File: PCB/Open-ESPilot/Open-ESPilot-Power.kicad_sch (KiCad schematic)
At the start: 32 parts, among them J2 VOUT, J3 VIN, J4 GND, M1 Clone "MP1584" module, Q1 AO3401A, U2 AMS1117-3.3, U3 AMS1117-3.3, U4 INA219AxD

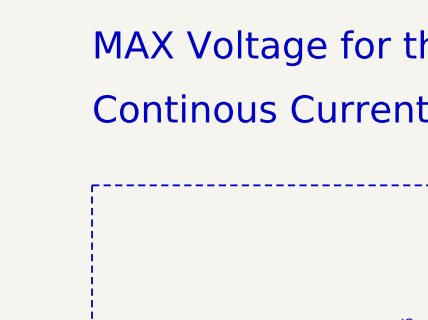
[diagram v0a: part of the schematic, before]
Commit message: Selected componets and tried to made a csv.
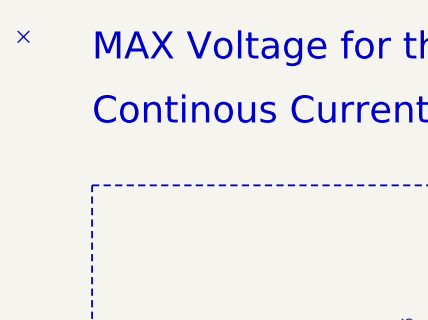
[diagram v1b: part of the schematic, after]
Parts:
- C12, C13, C14: LCSC (none) -> C49678
- C6, C7, C8, C9: LCSC (none) -> C5674
- J2, J3, J4, JP1, JP2, JP3: LCSC (none) -> -
- M1: LCSC (none) -> -; Non LCSC link (none) -> https://www.aliexpress.com/item/1005005870392716.html
- R10, R11, R12, R6: LCSC (none) -> C84376
- R5: LCSC (none) -> C84375
- R7, R9: LCSC (none) -> C96347
- U3: LCSC (none) -> C6186
- U4: LCSC (none) -> C1574856
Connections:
- no-connect marks 0 -> 1
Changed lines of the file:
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@@
 		(color 0 0 0 0)
 	)
+	(no_connect
+		(at 8.89 15.24)
+	)
 	(wire
 		(pts
@@
 			)
 		)
+		(property "LCSC" "C84376"
+			(at 261.62 58.42 0)
+			(effects
+				(font
+					(size 1.27 1.27)
+				)
+				(hide yes)
+			)
+		)
 		(pin "1"
 		)
@@
 			)
 		)
+		(property "LCSC" "-"
+			(at 270.51 73.66 90)
+			(effects
+				(font
+					(size 1.27 1.27)
+				)
+				(hide yes)
+			)
+		)
 		(pin "1"
 		)
@@
 			)
 		)
+		(property "LCSC" "-"
+			(at 54.61 81.28 0)
+			(effects
+				(font
+					(size 1.27 1.27)
+				)
+				(hide yes)
+			)
+		)
 		(pin "1"
 		)
@@
 			)
 		)
+		(property "LCSC" "C5674"
+			(at 69.85 129.54 0)
+			(effects
+				(font
+					(size 1.27 1.27)
+				)
+				(hide yes)
+			)
+		)
 		(pin "1"
 		)
@@
 			)
 		)
+		(property "LCSC" "C96347"
+			(at 209.55 41.91 0)
+			(effects
+				(font
+					(size 1.27 1.27)
+				)
+				(hide yes)
+			)
+		)
 		(pin "2"
 		)
@@
 			)
 		)
+		(property "LCSC" "C1574856"
+			(at 233.68 62.23 0)
+			(effects
+				(font
+					(size 1.27 1.27)
+				)
+				(hide yes)
+			)
+		)
 		(pin "6"
 		)
@@
 			)
 		)
+		(property "LCSC" "C49678"
+			(at 201.93 53.34 90)
+			(effects
+				(font
+					(size 1.27 1.27)
+				)
+				(hide yes)
+			)
+		)
 		(pin "1"
 		)
@@
 			)
 		)
+		(property "LCSC" "C5674"
+			(at 39.37 166.37 0)
+			(effects
+				(font
+					(size 1.27 1.27)
+				)
+				(hide yes)
+			)
+		)
 		(pin "1"
 		)
@@
 			)
 		)
+		(property "LCSC" "-"
+			(at 261.62 73.66 90)
+			(effects
+				(font
+					(size 1.27 1.27)
+				)
+				(hide yes)
+			)
+		)
 		(pin "1"
 		)
@@
 			)
 		)
-		(property "Datasheet" "https://www.aliexpress.com/item/1005005870392716.html"
+		(property "Datasheet" ""
 			(at 138.43 111.252 0)
 			(effects
@@
 			)
 		)
+		(property "LCSC" "-"
+			(at 138.43 123.19 0)
+			(effects
+				(font
+					(size 1.27 1.27)
+				)
+				(hide yes)
+			)
+		)
+		(property "Non LCSC link" "https://www.aliexpress.com/item/1005005870392716.html"
+			(at 138.43 123.19 0)
+			(effects
+				(font
+					(size 1.27 1.27)
+				)
+				(hide yes)
+			)
+		)
 		(pin "3"
 		)
@@
 			)
 		)
+		(property "LCSC" "-"
+			(at 201.93 137.16 0)
+			(effects
+				(font
+					(size 1.27 1.27)
+				)
+				(hide yes)
+			)
+		)
 		(pin "1"
 		)
@@
 			)
 		)
+		(property "LCSC" "C5674"
+			(at 69.85 166.37 0)
+			(effects
+				(font
+					(size 1.27 1.27)
+				)
+				(hide yes)
+			)
+		)
 		(pin "1"
 		)
@@
 			)
 		)
+		(property "LCSC" "-"
+			(at 54.61 60.96 0)
+			(effects
+				(font
+					(size 1.27 1.27)
+				)
+				(hide yes)
+			)
+		)
 		(pin "1"
 		)
@@
 			)
 		)
+		(property "LCSC" "C5674"
+			(at 39.37 129.54 0)
+			(effects
+				(font
+					(size 1.27 1.27)
+				)
+				(hide yes)
+			)
+		)
 		(pin "1"
 		)
@@
 			)
 		)
+		(property "LCSC" "C84376"
+			(at 243.84 140.97 0)
+			(effects
+				(font
+					(size 1.27 1.27)
+				)
+				(hide yes)
+			)
+		)
 		(pin "2"
 		)
@@
 			)
 		)
+		(property "LCSC" "C49678"
+			(at 209.55 80.01 0)
+			(effects
+				(font
+					(size 1.27 1.27)
+				)
+				(hide yes)
+			)
+		)
 		(pin "2"
 		)
@@
 			)
 		)
+		(property "LCSC" "C49678"
+			(at 142.24 170.18 0)
+			(effects
+				(font
+					(size 1.27 1.27)
+				)
+				(hide yes)
+			)
+		)
 		(pin "2"
 		)
@@
 			)
 		)
+		(property "LCSC" "-"
+			(at 54.61 46.99 0)
+			(effects
+				(font
+					(size 1.27 1.27)
+				)
+				(hide yes)
+			)
+		)
 		(pin "1"
 		)
@@
 			)
 		)
+		(property "LCSC" "C84376"
+			(at 270.51 58.42 0)
+			(effects
+				(font
+					(size 1.27 1.27)
+				)
+				(hide yes)
+			)
+		)
 		(pin "1"
 		)
@@
 			)
 		)
+		(property "LCSC" "C84375"
+			(at 170.18 60.96 0)
+			(effects
+				(font
+					(size 1.27 1.27)
+				)
+				(hide yes)
+			)
+		)
 		(pin "1"
 		)
@@
 			)
 		)
+		(property "LCSC" "C96347"
+			(at 194.31 41.91 0)
+			(effects
+				(font
+					(size 1.27 1.27)
+				)
+				(hide yes)
+			)
+		)
 		(pin "2"
 		)
@@
 			)
 		)
+		(property "LCSC" "C6186"
+			(at 54.61 161.29 0)
+			(effects
+				(font
+					(size 1.27 1.27)
+				)
+				(hide yes)
+			)
+		)
 		(pin "2"
 		)
@@
 			(at 170.18 73.66 0)
 			(effects
+				(font
+					(size 1.27 1.27)
+				)
+				(hide yes)
+			)
+		)
+		(property "LCSC" "C84376"
+			(at 170.18 73.66 0)
+			(effects

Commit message: in dabenginging of V1.1
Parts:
- added D6: 3V3 IG, Diode_SMD:D_SOD-128, symbol Device:D_Zener
- JP6: renamed from JP1; footprint Connector_PinHeader_2.54mm:PinHeader_1x03_P2.54mm_Vertical -> Jumper:SolderJumper-3_P1.3mm_Open_RoundedPad1.0x1.5mm; now in the parts list
- renumbered JP2 to JP1, JP3 to JP2
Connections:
- net +5V: now also D6.1 (K); no longer C10.1
- net +5Vreg: now also C10.1
- net GND: now also D6.2 (A)
- no-connect marks 1 -> 0
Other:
- moved on the sheet: C6, C7, C8, C9, D4, JP6, Q1, R10, U2, U3
